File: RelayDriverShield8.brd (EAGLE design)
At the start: 62.2 x 69.8 mm, 76 parts, among them IC1 MCP23017SO, J1 Analog, J2 POWER, J3 Digital_0_7, J4 M100.1, J5 ICSPPTH, J7 PWR SELECT, Q1 2N7002, Q2 2N7002, Q3 2N7002, Q4 2N7002, Q5 2N7002, Q6 2N7002, Q7 2N7002, Q8 2N7002

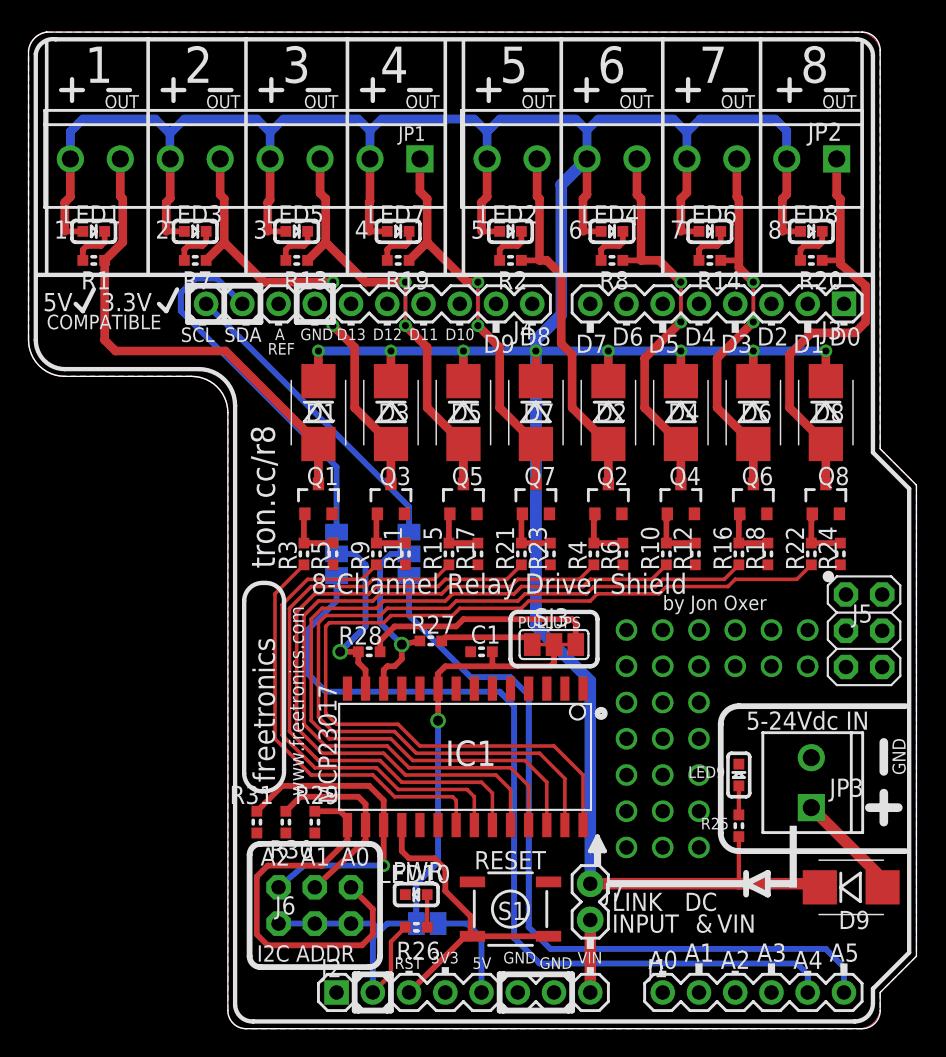
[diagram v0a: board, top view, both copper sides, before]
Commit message: Replaced parts using SuperHouse library to add 3D models
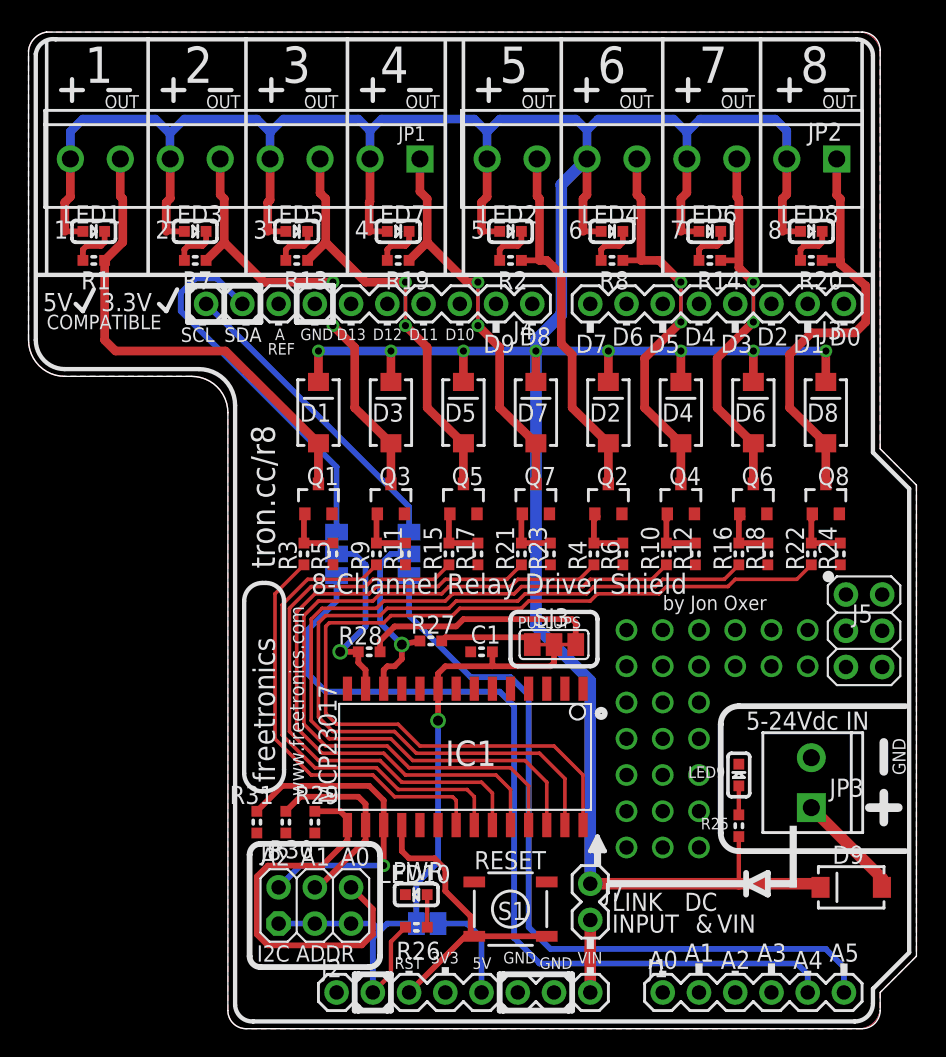
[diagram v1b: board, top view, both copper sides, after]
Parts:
- removed J6: (no value), freetronics-master-v1.1:2X03
- added J8: M02X3-PIN, SuperHouse-Connectors:2X03-P
- C1: device freetronics-original:0603 -> SuperHouse-DiscreteSemi:C0603
- D1, D2, D3, D4, D5, D6, D7, D8, D9: device freetronics-master-v1.1:SMB-DIODE -> SuperHouse-DiscreteSemi:SMA-DIODE
- IC1: device microchip:SO28W -> SuperHouse-ICs:SO28W
- J1: device freetronics:1X06 -> SuperHouse-Connectors:1X06-ST
- J2, J3: device freetronics:1X08 -> SuperHouse-Connectors:1X08-ST
- J4: value M100.1 -> M10-STACKING; device freetronics-original:1X10 -> SuperHouse-Connectors:1X10-ST
- J5: value ICSPPTH -> ICSP-ST-BELOW; device freetronics-jon:2X03PTH -> SuperHouse-Connectors:2X03-ICSP-ST-BELOW
- J7: device SparkFun:1X02 -> SuperHouse-Connectors:1X02-P
- JP1, JP2: value (none) -> M08-SCREW-3.5MM; device freetronics-master-v1:TERMINALBLOCK_3.5MM_8 -> SuperHouse-Connectors:SCREWTERMINAL_3.5MM_8
- JP3: device freetronics-master-v1.1:SCREWTERMINAL-3.5MM-2 -> SuperHouse-Connectors:SCREWTERMINAL-3.5MM-2
- LED1, LED10, LED2, LED3, LED4, LED5, LED6, LED7, LED8, LED9: device freetronics-master-v1:LED-0603 -> SuperHouse-LEDs:LED-0603
- Q1, Q2, Q3, Q4, Q5, Q6, Q7, Q8: device freetronics-master-v1:SOT23-3 -> SuperHouse-DiscreteSemi:SOT23-3
- R1, R10, R11, R12, R13, R14, R15, R16, R17, R18, R19, R2, R20, R21, R22, R23, R24, R25, R26, R27, R28, R29, R3, R30, R31, R4, R5, R6, R7, R8, R9: device freetronics-master-v1:0603 -> SuperHouse-DiscreteSemi:R0603
- S1: device freetronics-original:TACTILE_SWITCH_SMD -> SuperHouse-Switches:TACTILE_SMT-6MM
- turned D1 to 90 degrees
- turned D2 to 90 degrees
- turned D3 to 90 degrees
- turned D4 to 90 degrees
- turned D5 to 90 degrees
- turned D6 to 90 degrees
- turned D7 to 90 degrees
- turned D8 to 90 degrees
- turned D9 to 180 degrees
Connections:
- net ADDR0: now also J8.6; no longer J6.2
- net ADDR1: now also J8.4; no longer J6.4
- net ADDR2: now also J8.2; no longer J6.6
- net IOREF: now also J8.1, J8.3, J8.5; no longer J6.1, J6.3, J6.5
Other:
- board text added: "(c) 2012-19 Freetronics Pty Ltd"
- board text added: "8-Channel Relay Driver Shield v2.1"
- board text removed: "(c) 2012-14 Freetronics Pty Ltd"
- board text removed: "8-Channel Relay Driver Shield v2.0"
